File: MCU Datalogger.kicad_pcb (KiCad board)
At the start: 4 copper layers, 53.8 x 35.8 mm, 30 parts, among them J1 Conn_01x04_Pin, J2 Conn_01x09_Pin, J3 Conn_01x04_Pin, J4 Conn_02x03_Odd_Even, U1 24LC1025, U2 24LC1025, U3 DS1337S_, U4 ATMEGA328P-AU, Y1 32.768 KHz, Y2 16 MHz

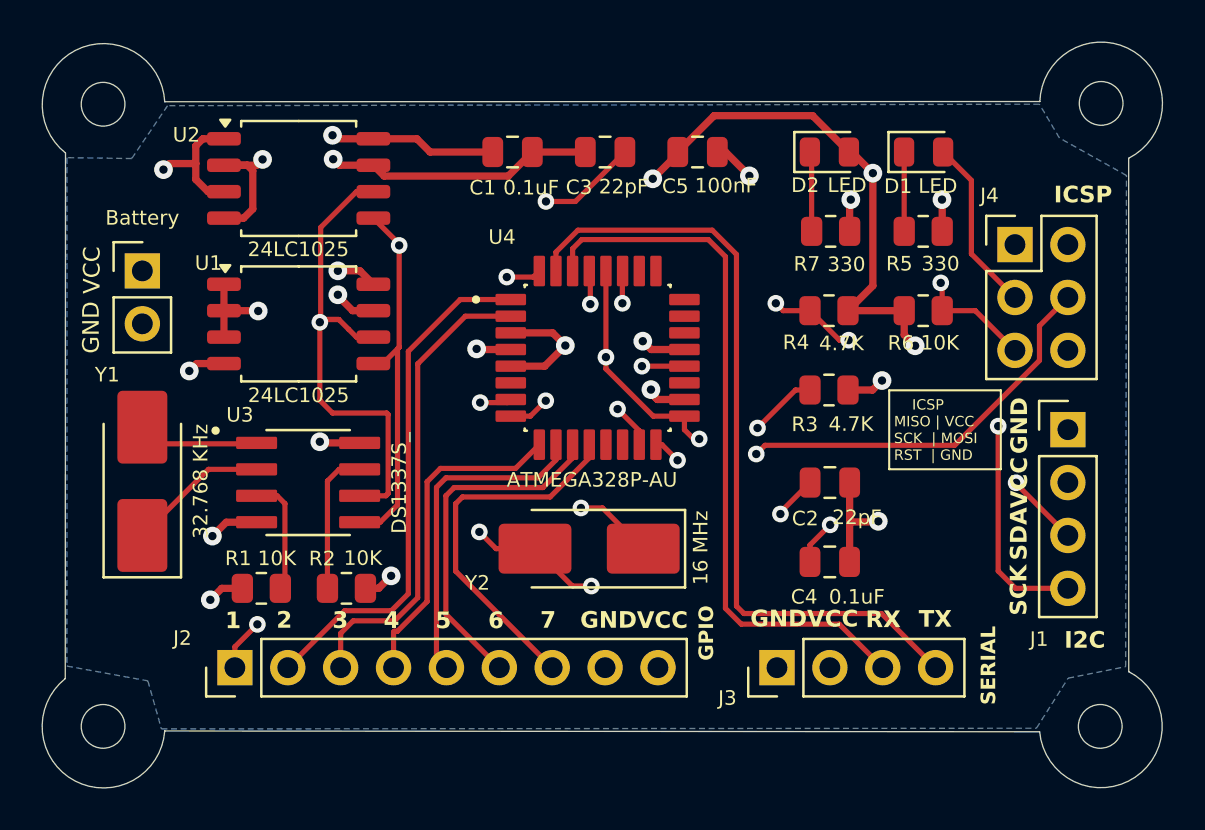
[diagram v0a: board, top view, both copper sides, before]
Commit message: Fixed Bugs in the 4layer PCB
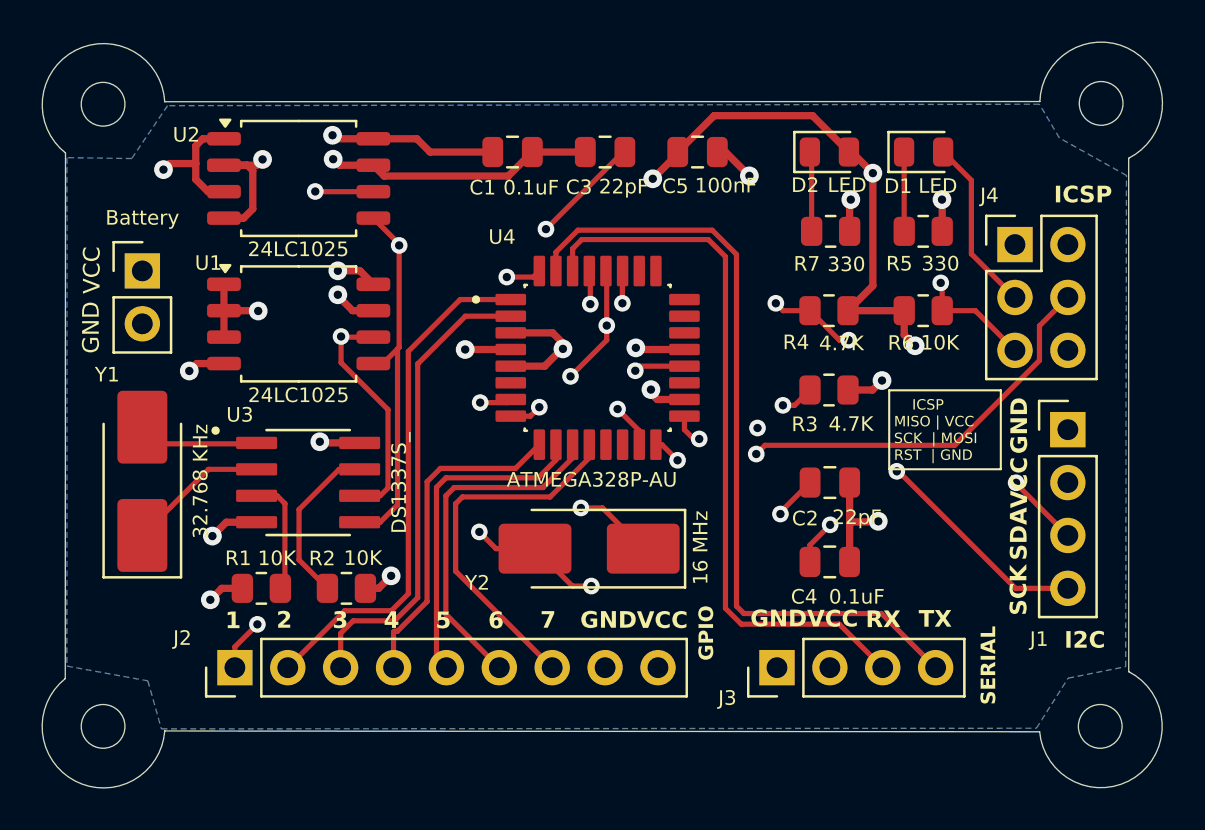
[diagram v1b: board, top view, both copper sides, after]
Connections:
- J1 pad 4: /SCK -> /SCL
- R3 pad 2: /SCK -> /SCL
- U1 pad 6: /SCK -> /SCL
- U2 pad 6: /SCK -> /SCL
- U3 pad 6: /SCK -> /SCL
- U4 pad 28: /SCK -> /SCL
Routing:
- net /SCL: track 0.00 -> 70.5 mm, vias 0 -> 6
- net /SCK: track 97.1 -> 28.0 mm, vias 5 -> 2
- net Net-(U3-SQW/~INT): track 6.93 -> 8.06 mm
- net Net-(U4-PB7): track 26.0 -> 25.0 mm
- net Net-(U4-AREF): track 17.7 -> 18.3 mm
- net /Vcc: track 55.9 -> 56.4 mm

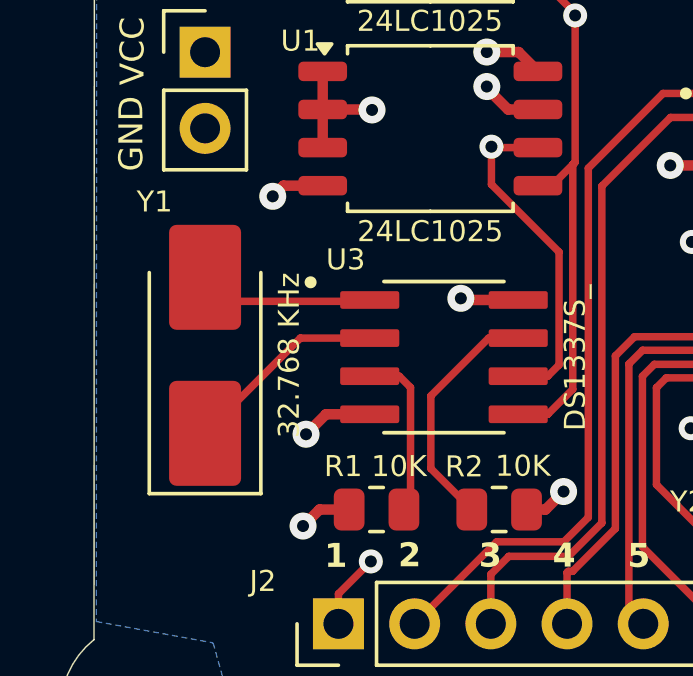
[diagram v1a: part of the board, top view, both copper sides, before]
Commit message: Changed 32.768khz oscillator footprint from 5032 to 3215
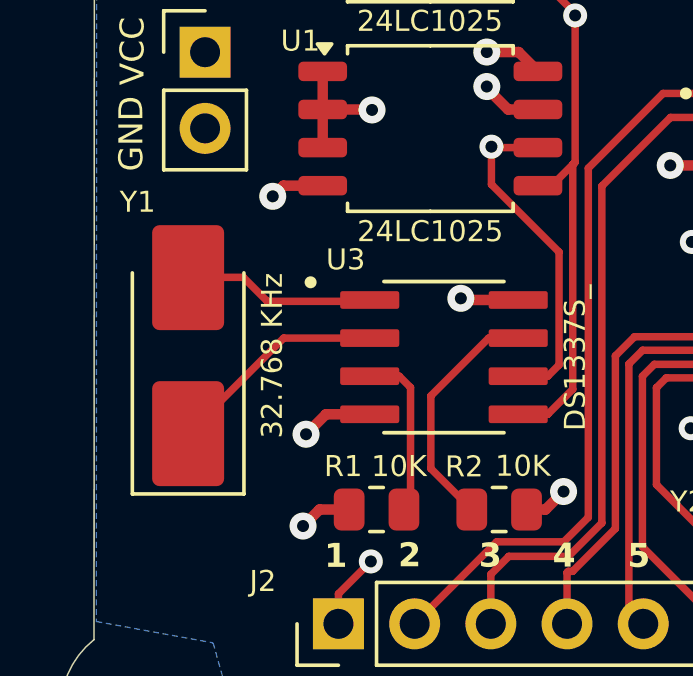
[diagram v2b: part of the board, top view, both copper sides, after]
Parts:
- moved Y1 0.57 mm to (67.4, 86.3)
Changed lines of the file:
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@@
 	(footprint "Crystal:Crystal_SMD_5032-2Pin_5.0x3.2mm_HandSoldering"
 		(layer "F.Cu")
-		(at 67.945 86.3 90)
+		(at 67.38 86.31 90)
 		(descr "SMD2520/2, Crystal, 5.0x3.2mm package, SMD, hand-soldering, generated with kicad-footprint-generator make_crystal.py, http://www.icbase.com/File/PDF/HKC/HKC00061008.pdf")
 		(property "Reference" "Y1"
@@
 	)
 	(segment
-		(start 68.745 84.5)
+		(start 70.02 84.5)
 		(end 73.3875 84.5)
 		(width 0.25)
@@
 	(segment
 		(start 67.945 83.7)
-		(end 68.745 84.5)
+		(end 69.22 83.7)
 		(width 0.25)
 		(layer "F.Cu")
@@
 	)
 	(segment
-		(start 67.945 88.9)
-		(end 71.12 85.725)
+		(start 69.22 83.7)
+		(end 70.02 84.5)
 		(width 0.25)
 		(layer "F.Cu")
-		(net 25)
+		(net 24)
 	)
 	(segment
-		(start 71.12 85.725)
+		(start 70.565 85.725)
 		(end 73.4325 85.725)
 		(width 0.25)
 		(layer "F.Cu")
+		(net 25)
+	)
+	(segment
+		(start 67.945 88.345)
+		(end 70.565 85.725)
+		(width 0.25)
+		(layer "F.Cu")
+		(net 25)
+	)
+	(segment
+		(start 67.945 88.9)
+		(end 67.945 88.345)
+		(width 0.25)
+		(layer "F.Cu")

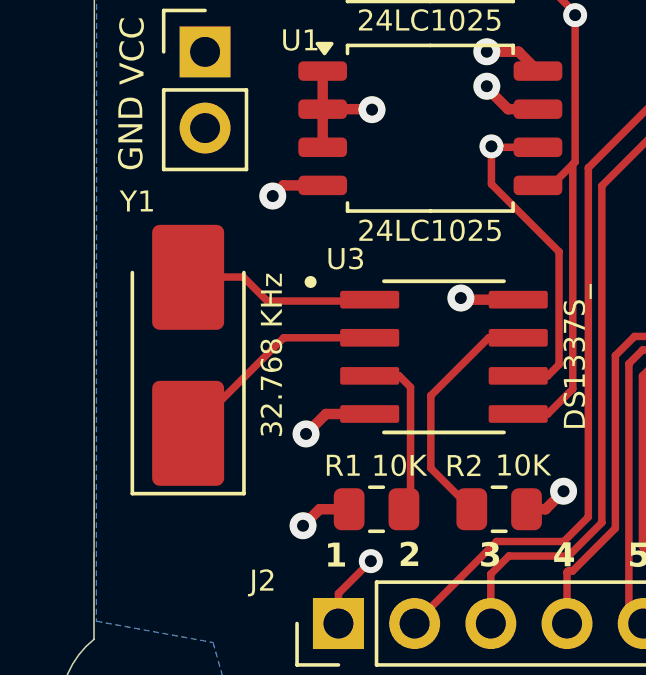
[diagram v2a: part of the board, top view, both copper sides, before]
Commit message: Updated 3215 32.768kHz Oscillator in the 4layer PCB
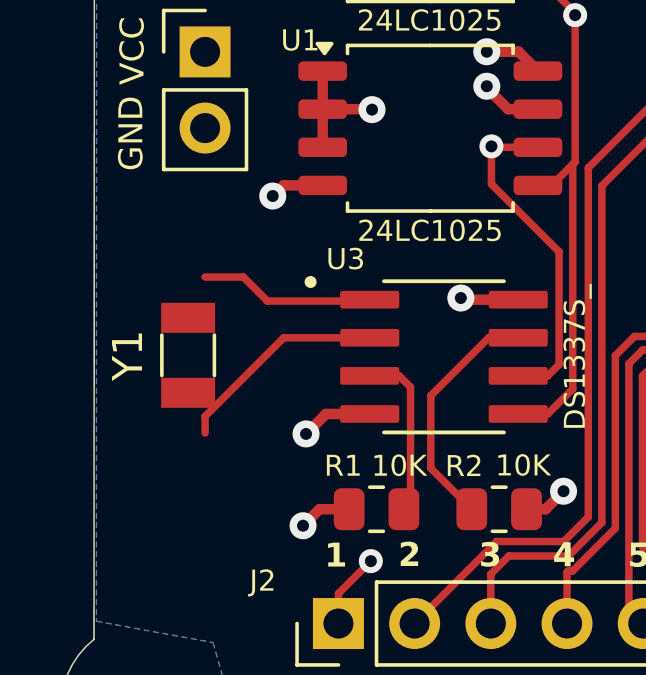
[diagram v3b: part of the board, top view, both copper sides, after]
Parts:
- Y1: footprint Crystal:Crystal_SMD_5032-2Pin_5.0x3.2mm_HandSoldering -> Crystal:Crystal_SMD_3215-2Pin_3.2x1.5mm
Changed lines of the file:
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@@
 		)
 	)
-	(footprint "Crystal:Crystal_SMD_5032-2Pin_5.0x3.2mm_HandSoldering"
+	(footprint "Crystal:Crystal_SMD_3215-2Pin_3.2x1.5mm"
 		(layer "F.Cu")
 		(at 67.38 86.31 90)
-		(descr "SMD2520/2, Crystal, 5.0x3.2mm package, SMD, hand-soldering, generated with kicad-footprint-generator make_crystal.py, http://www.icbase.com/File/PDF/HKC/HKC00061008.pdf")
+		(descr "SMD Crystal FC-135 https://support.epson.biz/td/api/doc_check.php?dl=brief_FC-135R_en.pdf")
+		(tags "SMD SMT Crystal")
 		(property "Reference" "Y1"
-			(at 5.12 -1.685 180)
+			(at 0 -2 90)
 			(layer "F.SilkS")
 			(effects
 				(font
-					(size 0.7 0.7)
-					(thickness 0.1)
+					(size 1 1)
+					(thickness 0.15)
 				)
 			)
 		)
 		(property "Value" "32.768 KHz"
-			(at 0 2.8 90)
-			(layer "F.SilkS")
+			(at 0 2 90)
+			(layer "F.Fab")
 			(effects
 				(font
-					(size 0.7 0.7)
-					(thickness 0.1)
+					(size 1 1)
+					(thickness 0.15)
 				)
 			)
@@
 		(property "Datasheet" "~"
 			(at 0 0 90)
+			(unlocked yes)
 			(layer "F.Fab")
 			(hide yes)
@@
 		(property "Description" "Two pin crystal"
 			(at 0 0 90)
+			(unlocked yes)
 			(layer "F.Fab")
 			(hide yes)
@@
 		(attr smd)
 		(fp_line
-			(start 2.76 -1.86)
-			(end -4.61 -1.86)
+			(start -0.675 -0.875)
+			(end 0.675 -0.875)
 			(stroke
 				(width 0.12)
@@
 		)
 		(fp_line
-			(start -4.61 -1.86)
-			(end -4.61 1.86)
+			(start -0.675 0.875)
+			(end 0.675 0.875)
 			(stroke
 				(width 0.12)
@@
 		)
 		(fp_line
-			(start -4.61 1.86)
-			(end 2.76 1.86)
+			(start 2 -1.15)
+			(end 2 1.15)
 			(stroke
-				(width 0.12)
+				(width 0.05)
 				(type solid)
 			)
-			(layer "F.SilkS")
+			(layer "F.CrtYd")
 		)
-		(fp_circle
-			(center 0 0)
-			(end 0.4 0)
+		(fp_line
+			(start -2 -1.15)
+			(end 2 -1.15)
+			(stroke
+				(width 0.05)
+				(type solid)
+			)
+			(layer "F.CrtYd")
+		)
+		(fp_line
+			(start -2 -1.15)
+			(end -2 1.15)
+			(stroke
+				(width 0.05)
+				(type solid)
+			)
+			(layer "F.CrtYd")
+		)
+		(fp_line
+			(start -2 1.15)
+			(end 2 1.15)
+			(stroke
+				(width 0.05)
+				(type solid)
+			)
+			(layer "F.CrtYd")
+		)
+		(fp_line
+			(start 1.6 -0.75)
+			(end 1.6 0.75)
 			(stroke
 				(width 0.1)
 				(type solid)
 			)
-			(fill yes)
-			(layer "F.Adhes")
+			(layer "F.Fab")
 		)
-		(fp_rect
-			(start -4.6 -2.1)
-			(end 4.6 2.1)
-			(stroke
-				(width 0.05)
-				(type solid)
-			)
-			(fill no)
-			(layer "F.CrtYd")
-		)
-		(fp_poly
-			(pts
-				(xy -2.5 -1.6) (xy -2.5 0.8) (xy -1.7 1.6) (xy 2.5 1.6) (xy 2.5 -1.6)
-			)
+		(fp_line
+			(start -1.6 -0.75)
+			(end 1.6 -0.75)
 			(stroke
 				(width 0.1)
 				(type solid)
 			)
-			(fill no)
+			(layer "F.Fab")
+		)
+		(fp_line
+			(start -1.6 -0.75)
+			(end -1.6 0.75)
+			(stroke
+				(width 0.1)
+				(type solid)
+			)
+			(layer "F.Fab")
+		)
+		(fp_line
+			(start -1.6 0.75)
+			(end 1.6 0.75)
+			(stroke
+				(width 0.1)
+				(type solid)
+			)
 			(layer "F.Fab")
 		)
 		(fp_text user "${REFERENCE}"
-			(at 0 0 90)
+			(at 0 -2 90)
 			(layer "F.Fab")
 			(effects
 				(font
-					(size 0.7 0.7)
-					(thickness 0.1)
+					(size 1 1)
+					(thickness 0.15)
 				)
 			)
 		)
-		(pad "1" smd roundrect
-			(at -2.6 0 90)
-			(size 3.5 2.4)
+		(pad "1" smd rect
+			(at 1.25 0 90)
+			(size 1 1.8)
 			(layers "F.Cu" "F.Mask" "F.Paste")
-			(roundrect_rratio 0.104167)
 			(net 25 "Net-(U3-X2)")
 			(pinfunction "1")
 			(pintype "passive")
 		)
-		(pad "2" smd roundrect
-			(at 2.6 0 90)
-			(size 3.5 2.4)
+		(pad "2" smd rect
+			(at -1.25 0 90)
+			(size 1 1.8)
 			(layers "F.Cu" "F.Mask" "F.Paste")
-			(roundrect_rratio 0.104167)
 			(net 24 "Net-(U3-X1)")
 			(pinfunction "2")
@@
 		)
 		(embedded_fonts no)
-		(model "${KICAD9_3DMODEL_DIR}/Crystal.3dshapes/Crystal_SMD_5032-2Pin_5.0x3.2mm.step"
+		(model "${KICAD9_3DMODEL_DIR}/Crystal.3dshapes/Crystal_SMD_3215-2Pin_3.2x1.5mm.step"
 			(offset
 				(xyz 0 0 0)

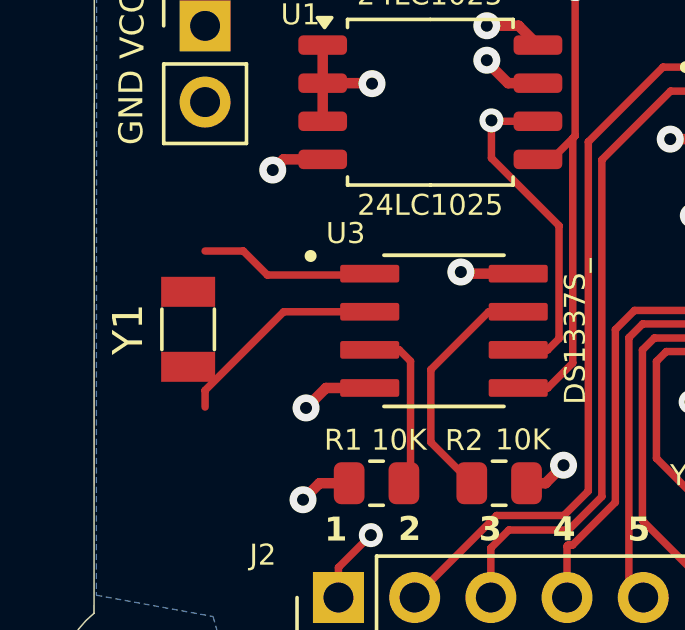
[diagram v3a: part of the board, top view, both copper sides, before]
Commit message: Updated 3215 32.768kHz Oscillator in the 4layer PCB
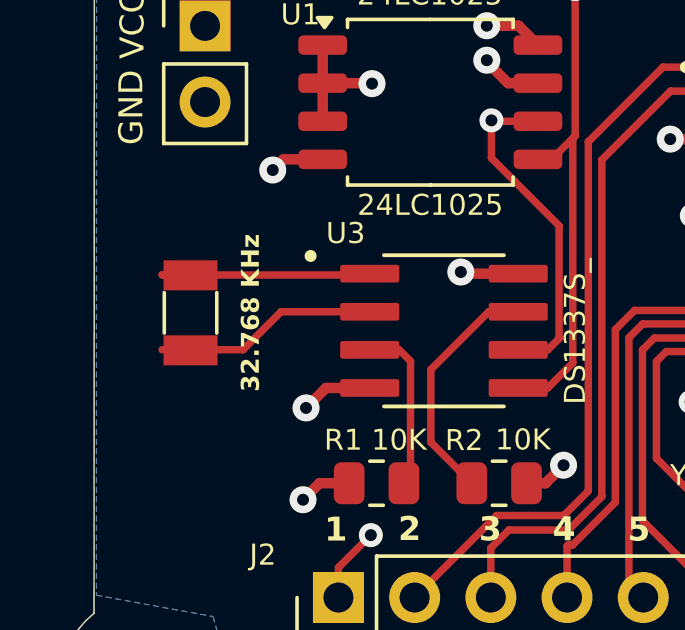
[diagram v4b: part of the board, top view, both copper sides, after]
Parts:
- 32.768 KHz: renamed from Y1; value 32.768 KHz -> 32.768
- moved 32.768 KHz 0.56 mm to (67.5, 85.8), turned to -90 degrees
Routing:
- net Net-(U3-X1): track 5.84 -> 6.95 mm
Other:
- board text added: "KHz"
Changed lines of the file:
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@@
 	(footprint "Crystal:Crystal_SMD_3215-2Pin_3.2x1.5mm"
 		(layer "F.Cu")
-		(at 67.38 86.31 90)
+		(at 67.46 85.76 -90)
 		(descr "SMD Crystal FC-135 https://support.epson.biz/td/api/doc_check.php?dl=brief_FC-135R_en.pdf")
 		(tags "SMD SMT Crystal")
-		(property "Reference" "Y1"
+		(property "Reference" "32.768 KHz"
 			(at 0 -2 90)
 			(layer "F.SilkS")
 			(effects
 				(font
-					(size 1 1)
-					(thickness 0.15)
+					(size 0.6 0.6)
+					(thickness 0.12)
+					(bold yes)
 				)
 			)
 		)
-		(property "Value" "32.768 KHz"
-			(at 0 2 90)
+		(property "Value" "32.768"
+			(at 2.61 -0.23 180)
 			(layer "F.Fab")
 			(effects
 				(font
-					(size 1 1)
+					(size 0.6 0.6)
 					(thickness 0.15)
 				)
@@
 		)
 		(property "Datasheet" "~"
-			(at 0 0 90)
+			(at 0 0 270)
 			(unlocked yes)
 			(layer "F.Fab")
@@
 		)
 		(property "Description" "Two pin crystal"
-			(at 0 0 90)
+			(at 0 0 270)
 			(unlocked yes)
 			(layer "F.Fab")
@@
 		)
 		(property "Purpose" ""
-			(at 0 0 90)
+			(at 0 0 270)
 			(unlocked yes)
 			(layer "F.Fab")
@@
 		(attr smd)
 		(fp_line
-			(start -0.675 -0.875)
-			(end 0.675 -0.875)
+			(start -0.675 0.875)
+			(end 0.675 0.875)
 			(stroke
 				(width 0.12)
@@
 		)
 		(fp_line
-			(start -0.675 0.875)
-			(end 0.675 0.875)
+			(start -0.675 -0.875)
+			(end 0.675 -0.875)
 			(stroke
 				(width 0.12)
@@
 		)
 		(fp_line
-			(start 2 -1.15)
+			(start -2 1.15)
 			(end 2 1.15)
 			(stroke
@@
 		(fp_line
 			(start -2 -1.15)
-			(end 2 -1.15)
+			(end -2 1.15)
 			(stroke
 				(width 0.05)
@@
 		(fp_line
 			(start -2 -1.15)
-			(end -2 1.15)
+			(end 2 -1.15)
 			(stroke
 				(width 0.05)
@@
 		)
 		(fp_line
-			(start -2 1.15)
+			(start 2 -1.15)
 			(end 2 1.15)
 			(stroke
@@
 		)
 		(fp_line
-			(start 1.6 -0.75)
+			(start -1.6 0.75)
 			(end 1.6 0.75)
 			(stroke
@@
 		(fp_line
 			(start -1.6 -0.75)
-			(end 1.6 -0.75)
+			(end -1.6 0.75)
 			(stroke
 				(width 0.1)
@@
 		(fp_line
 			(start -1.6 -0.75)
-			(end -1.6 0.75)
+			(end 1.6 -0.75)
 			(stroke
 				(width 0.1)
@@
 		)
 		(fp_line
-			(start -1.6 0.75)
+			(start 1.6 -0.75)
 			(end 1.6 0.75)
 			(stroke
@@
 		)
 		(fp_text user "${REFERENCE}"
-			(at 0 -2 90)
+			(at -2.87 -0.35 90)
 			(layer "F.Fab")
 			(effects
@@
 		)
 		(pad "1" smd rect
-			(at 1.25 0 90)
+			(at 1.25 0 270)
 			(size 1 1.8)
 			(layers "F.Cu" "F.Mask" "F.Paste")
@@
 		)
 		(pad "2" smd rect
-			(at -1.25 0 90)
+			(at -1.25 0 270)
 			(size 1 1.8)
 			(layers "F.Cu" "F.Mask" "F.Paste")
@@
 		)
 	)
+	(gr_text "KHz"
+		(at 67.35 89.31 0)
+		(layer "F.Fab")
+		(effects
+			(font
+				(size 0.6 0.6)
+				(thickness 0.15)
+			)
+		)
+	)
 	(gr_text "Copper Layer Count: "
 		(at 125.642857 76.94 0)
@@
 	)
 	(segment
-		(start 70.02 84.5)
+		(start 66.52 84.5)
 		(end 73.3875 84.5)
 		(width 0.25)
@@
 	)
 	(segment
-		(start 67.945 83.7)
-		(end 69.22 83.7)
+		(start 66.51 84.49)
+		(end 66.52 84.5)
 		(width 0.25)
 		(layer "F.Cu")
@@
 	)
 	(segment
-		(start 69.22 83.7)
-		(end 70.02 84.5)
-		(width 0.25)
-		(layer "F.Cu")
-		(net 24)
-	)
-	(segment
-		(start 70.565 85.725)
-		(end 73.4325 85.725)
+		(start 66.51 86.99)
+		(end 69.21 86.99)
 		(width 0.25)
 		(layer "F.Cu")
@@
 	)
 	(segment
-		(start 67.945 88.345)
-		(end 70.565 85.725)
+		(start 69.21 86.99)
+		(end 70.475 85.725)
 		(width 0.25)
 		(layer "F.Cu")
@@
 	)
 	(segment
-		(start 67.945 88.9)
-		(end 67.945 88.345)
+		(start 70.475 85.725)
+		(end 73.4325 85.725)
 		(width 0.25)
 		(layer "F.Cu")
